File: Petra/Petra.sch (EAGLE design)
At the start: 26 parts, among them J2 AVR_SPI_PRG_6NS, U1 MIC5219 5V, Y1 16MHz

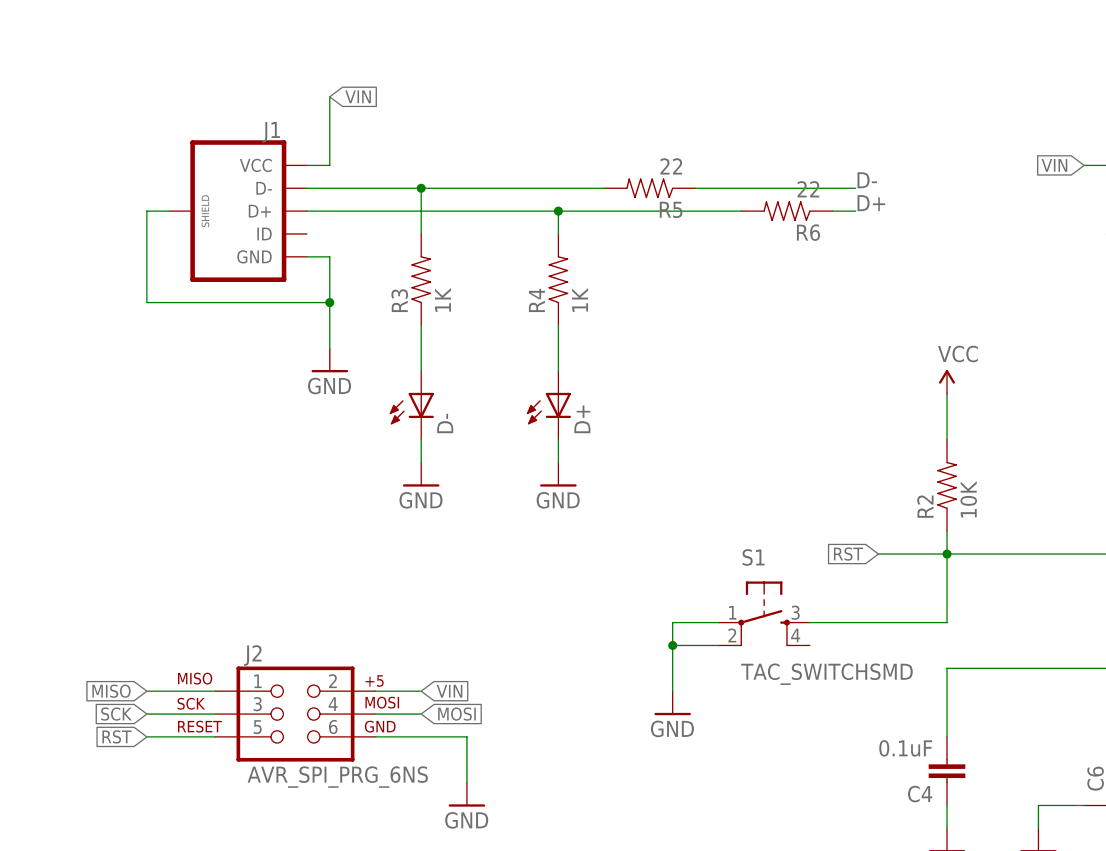
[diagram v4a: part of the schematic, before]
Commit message: Changed usb and button part. Reduced board size even further.
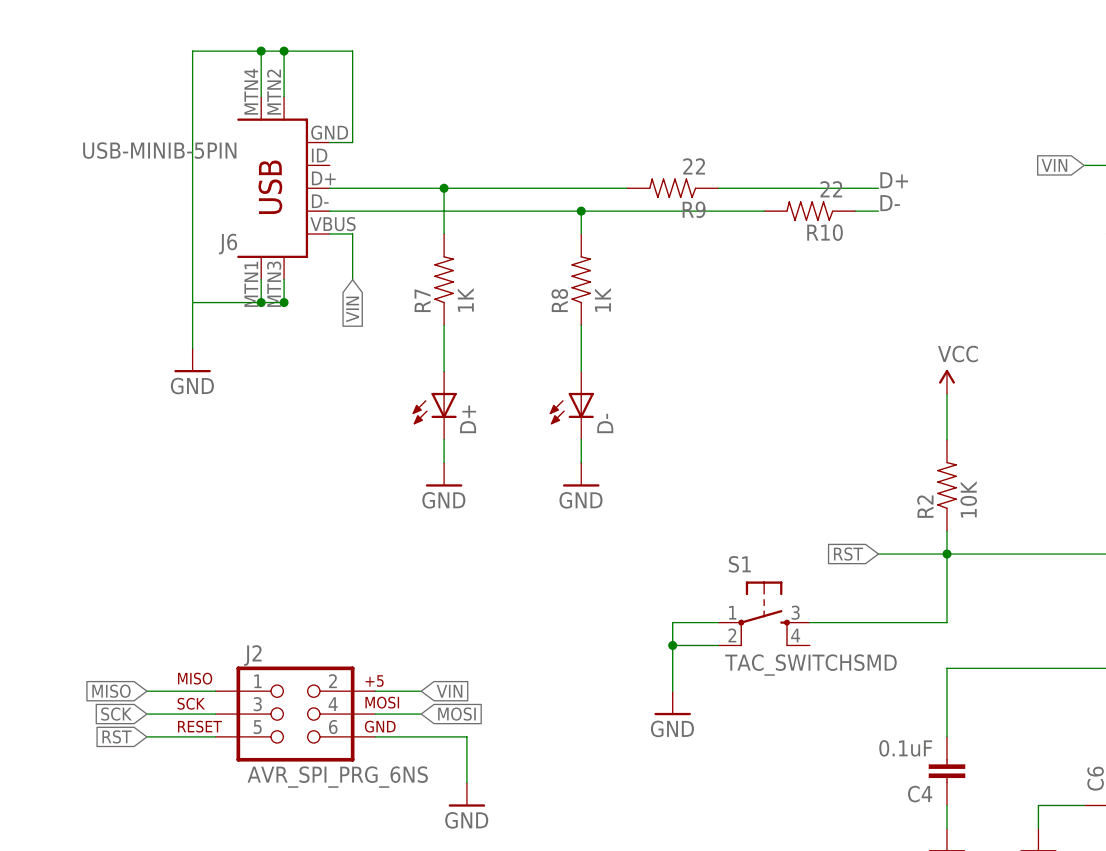
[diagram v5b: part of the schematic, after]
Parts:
- removed J1: (no value), SparkFun-Connectors:USB_MICROB_PLUGCONN-11752
- removed R3, R4: 1K, SparkFun-Resistors:10KOHM-1/10W-1%(0603)0603
- removed R5, R6: 22, SparkFun-Resistors:10KOHM-1/10W-1%(0603)0603
- added J6: USB-MINIB-5PIN, SparkFun-Connectors:USB-MINIB-5PIN
- added R10, R9: 22, SparkFun-Resistors:10KOHM-1/10W-1%(0603)0603
- added R7, R8: 1K, SparkFun-Resistors:10KOHM-1/10W-1%(0603)0603
- S1: device SparkFun-Retired:TAC_SWITCHSMD -> GeekAmmo:TACTILE-SWITCH-PTH
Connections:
- removed net N$11: D-.A, R3.1
- removed net N$5: J1.D-, R3.2, R5.2
- removed net N$6: J1.D+, R4.2, R6.2
- removed net N$9: D+.A, R4.1
- new net N$27: D-.A, R8.1
- new net N$28: D+.A, R7.1
- new net N$29: J6.D+, R7.2, R9.2
- new net N$30: J6.D-, R10.2, R8.2
- net D+: now also R9.1; no longer R6.1
- net D-: now also R10.1; no longer R5.1
- net GND: now also J6.GND, J6.MTN1, J6.MTN2, J6.MTN3, J6.MTN4; no longer J1.GND, J1.SHIELD
- net VIN: now also J6.VBUS; no longer J1.VCC
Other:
- moved on the sheet: D+, D-
